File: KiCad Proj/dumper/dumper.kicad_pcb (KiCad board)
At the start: 2 copper layers, 23 parts, among them J1 CartBus, J2 LINK PORT, K1 G6K-2, SW2 SW_SPST, SW3 SW_SPST, SW4 KFC-C-15A, U1 74HC595, U2 SN74LVC8T245PWR, U3 74HC595, U4 SN74LVC8T245PWR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

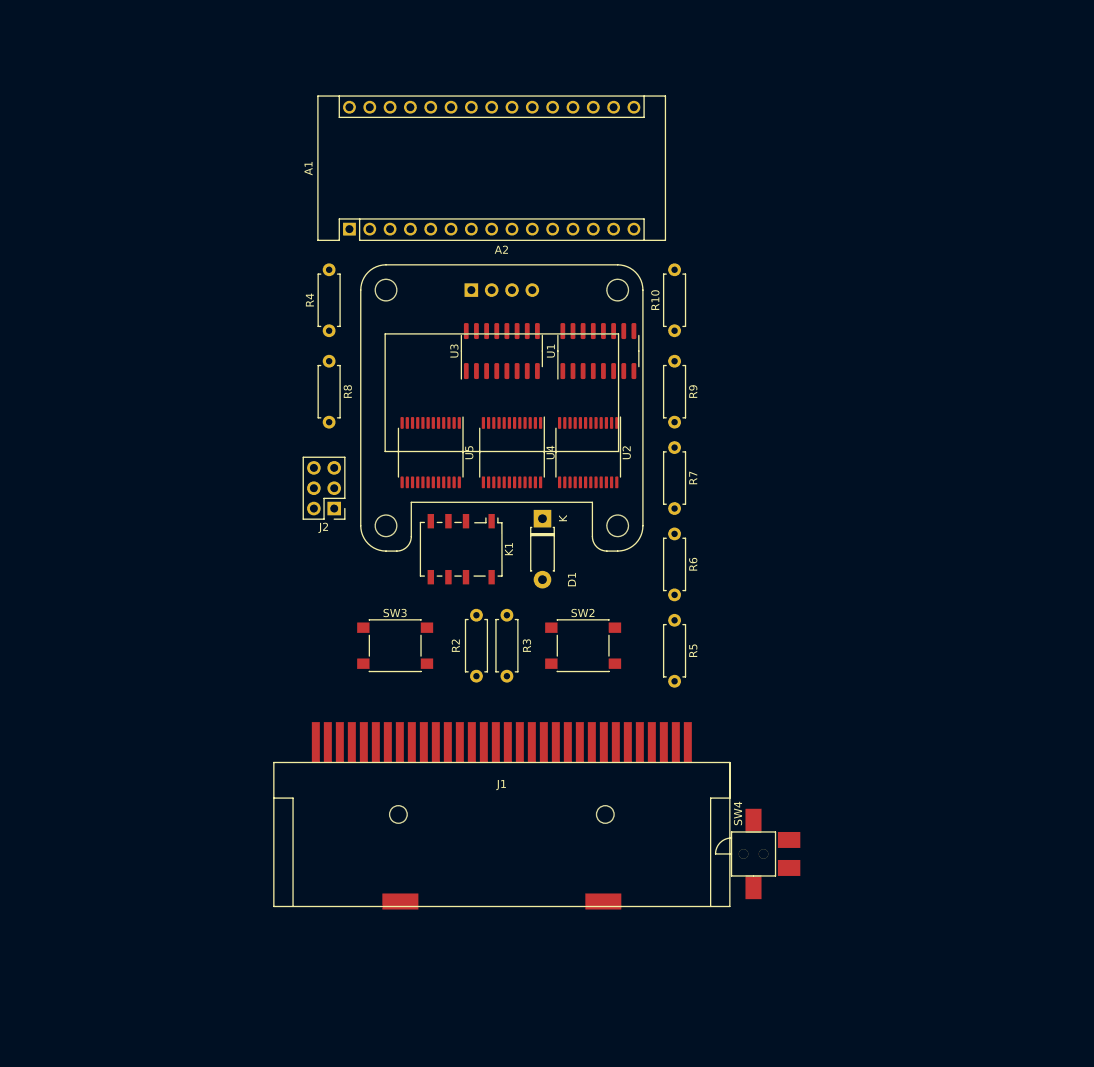
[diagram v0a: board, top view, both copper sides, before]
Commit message: Finalized schematic and PCB
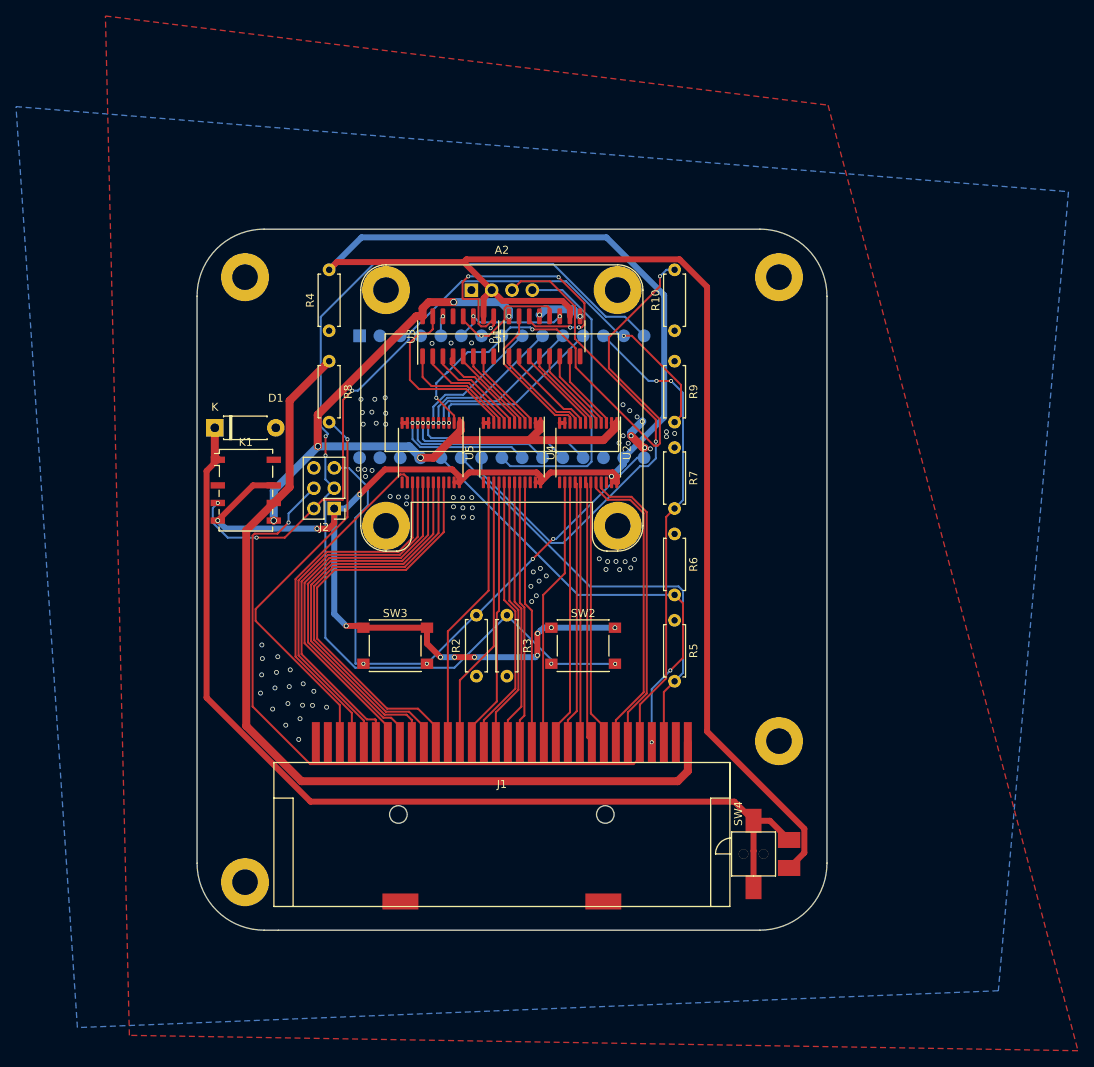
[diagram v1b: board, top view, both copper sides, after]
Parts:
- added REF**: MountingHole_3.2mm_M3_ISO7380_Pad, MountingHole:MountingHole_3.2mm_M3_ISO7380_Pad, F.Cu at (202.3, 117.3)
- added REF**: MountingHole_3.2mm_M3_ISO7380_Pad, MountingHole:MountingHole_3.2mm_M3_ISO7380_Pad, F.Cu at (135.5, 135.0)
- added REF**: MountingHole_3.2mm_M3_ISO7380_Pad, MountingHole:MountingHole_3.2mm_M3_ISO7380_Pad, F.Cu at (135.5, 59.3)
- added REF**: MountingHole_3.2mm_M3_ISO7380_Pad, MountingHole:MountingHole_3.2mm_M3_ISO7380_Pad, F.Cu at (202.3, 59.3)
- A1: footprint Module:Arduino_Nano -> Module:Arduino_Nano_SMD; moved to B.Cu
- J2: value LINK PORT -> SPI
- moved D1 42.5 mm to (131.8, 78.2), turned to 0 degrees
- moved K1 27.9 mm to (135.6, 86.0), turned to 0 degrees
- moved A1 13.4 mm to (149.9, 66.7), turned to 270 degrees
- moved U1 6.98 mm to (173.0, 66.7)
- moved U3 5.77 mm to (162.2, 66.7)
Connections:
- A2 pad : (no net) -> GND
- U1 pad 1: Net-(U1-Pad1) -> /Data I/O/QB_B
- U1 pad 14: /Controller/ADDRESS_DATA -> Net-(U1-Pad14)
- U1 pad 15: Net-(U1-Pad15) -> /Data I/O/QA_B
- U1 pad 16: +3V3 -> +5V
- U1 pad 2: Net-(U1-Pad2) -> /Data I/O/QC_B
- U1 pad 3: Net-(U1-Pad3) -> /Data I/O/QD_B
- U1 pad 4: Net-(U1-Pad4) -> /Data I/O/QE_B
- U1 pad 5: Net-(U1-Pad5) -> /Data I/O/QF_B
- U1 pad 6: Net-(U1-Pad6) -> /Data I/O/QG_B
- U1 pad 7: Net-(U1-Pad7) -> /Data I/O/QH_B
- U1 pad 8: Net-(U1-Pad8) -> GND
- U1 pad 9: Net-(U1-Pad9) -> GND
- U2 pad 1: +3V3 -> +5V
- U2 pad 10: Net-(U1-Pad7) -> /Data I/O/QA_B
- U2 pad 14: /Cartridge Slot/A0 -> /Cartridge Slot/A7
- U2 pad 15: /Cartridge Slot/A1 -> /Cartridge Slot/A6
- U2 pad 16: /Cartridge Slot/A2 -> /Cartridge Slot/A5
- U2 pad 17: /Cartridge Slot/A3 -> /Cartridge Slot/A4
- U2 pad 18: /Cartridge Slot/A4 -> /Cartridge Slot/A3
- U2 pad 19: /Cartridge Slot/A5 -> /Cartridge Slot/A2
- U2 pad 2: +3V3 -> +5V
- U2 pad 20: /Cartridge Slot/A6 -> /Cartridge Slot/A1
- U2 pad 21: /Cartridge Slot/A7 -> /Cartridge Slot/A0
- U2 pad 22: GND -> Net-(U2-Pad22)
- U2 pad 23: +5V -> +3V3
- U2 pad 24: +5V -> +3V3
- U2 pad 3: Net-(U1-Pad15) -> /Data I/O/QH_B
- U2 pad 4: Net-(U1-Pad1) -> /Data I/O/QG_B
- U2 pad 5: Net-(U1-Pad2) -> /Data I/O/QF_B
- U2 pad 6: Net-(U1-Pad3) -> /Data I/O/QE_B
- U2 pad 7: Net-(U1-Pad4) -> /Data I/O/QD_B
- U2 pad 8: Net-(U1-Pad5) -> /Data I/O/QC_B
- U2 pad 9: Net-(U1-Pad6) -> /Data I/O/QB_B
- U3 pad 1: Net-(U3-Pad1) -> /Data I/O/QB_A
- U3 pad 14: Net-(U1-Pad9) -> /Controller/ADDRESS_DATA
- U3 pad 15: Net-(U3-Pad15) -> /Data I/O/QA_A
- U3 pad 16: +3V3 -> +5V
- U3 pad 2: Net-(U3-Pad2) -> /Data I/O/QC_A
- U3 pad 3: Net-(U3-Pad3) -> /Data I/O/QD_A
- U3 pad 4: Net-(U3-Pad4) -> /Data I/O/QE_A
- U3 pad 5: Net-(U3-Pad5) -> /Data I/O/QF_A
- U3 pad 6: Net-(U3-Pad6) -> /Data I/O/QG_A
- U3 pad 7: Net-(U3-Pad7) -> /Data I/O/QH_A
- U3 pad 8: Net-(U3-Pad8) -> GND
- U3 pad 9: Net-(U3-Pad9) -> Net-(U1-Pad14)
- U4 pad 1: +3V3 -> +5V
- U4 pad 10: Net-(U3-Pad7) -> /Data I/O/QA_A
- U4 pad 14: /Cartridge Slot/A8 -> /Cartridge Slot/A15
- U4 pad 15: /Cartridge Slot/A9 -> /Cartridge Slot/A14
- U4 pad 16: /Cartridge Slot/A10 -> /Cartridge Slot/A13
- U4 pad 17: /Cartridge Slot/A11 -> /Cartridge Slot/A12
- U4 pad 18: /Cartridge Slot/A12 -> /Cartridge Slot/A11
- U4 pad 19: /Cartridge Slot/A13 -> /Cartridge Slot/A10
- U4 pad 2: +3V3 -> +5V
- U4 pad 20: /Cartridge Slot/A14 -> /Cartridge Slot/A9
- U4 pad 21: /Cartridge Slot/A15 -> /Cartridge Slot/A8
- U4 pad 23: +5V -> +3V3
- U4 pad 24: +5V -> +3V3
- U4 pad 3: Net-(U3-Pad15) -> /Data I/O/QH_A
- U4 pad 4: Net-(U3-Pad1) -> /Data I/O/QG_A
- U4 pad 5: Net-(U3-Pad2) -> /Data I/O/QF_A
- U4 pad 6: Net-(U3-Pad3) -> /Data I/O/QE_A
- U4 pad 7: Net-(U3-Pad4) -> /Data I/O/QD_A
- U4 pad 8: Net-(U3-Pad5) -> /Data I/O/QC_A
- U4 pad 9: Net-(U3-Pad6) -> /Data I/O/QB_A
- U5 pad 1: +3V3 -> +5V
- U5 pad 23: +5V -> +3V3
- U5 pad 24: +5V -> +3V3
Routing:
- net +3V3: track 0.00 -> 345.0 mm, vias 0 -> 12
- net /Cartridge Slot/CART_CS: track 0.00 -> 144.6 mm, vias 0 -> 3
- net /Controller/MISO: track 0.00 -> 131.8 mm, vias 0 -> 4
- net Net-(D1-Pad1): track 0.00 -> 123.4 mm
- net /Cart Detection/CART_VCC: track 0.00 -> 112.1 mm
- net +5V: track 0.00 -> 93.7 mm, vias 0 -> 5
- net /Cart Detection/GB_CART_H: track 0.00 -> 93.3 mm, vias 0 -> 4
- net /Controller/SCK: track 0.00 -> 74.7 mm, vias 0 -> 4
- net /Controller/SWITCH_TRANSCEIVER: track 0.00 -> 72.9 mm, vias 0 -> 3
- net /Controller/SCL: track 0.00 -> 64.5 mm, vias 0 -> 1
- net /Cartridge Slot/CART_RD: track 0.00 -> 56.8 mm, vias 0 -> 2
- net /Cartridge Slot/CART_WR: track 0.00 -> 54.5 mm
- net /Cartridge Slot/TD0: track 0.00 -> 52.7 mm
- net /Cartridge Slot/TD1: track 0.00 -> 51.5 mm
- net /Cartridge Slot/TD2: track 0.00 -> 50.9 mm
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- added copper zone on B.Cu, net GND
- added copper zone on F.Cu, net GND
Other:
- board outline added: 78.7 x 87.6 mm
- net class 3.3V added: clearance 0.127, trace_width 0.75, via_dia 0.6, via_drill 0.4
- net class 5V added: clearance 0.127, trace_width 1, via_dia 0.8, via_drill 0.6
- net class Default: clearance 0.2 -> 0.127; via_dia 0.8 -> 0.5; via_drill 0.4 -> 0.3
- net class GND added: clearance 0.127, trace_width 1, via_dia 0.8, via_drill 0.6
- rule pad_to_mask_clearance: 0 -> 0.05
- rule trace_clearance: 0.2 -> 0.127
- rule trace_min: 0.2 -> 0.21
- rule via_min_drill: 0.3 -> 0.2
